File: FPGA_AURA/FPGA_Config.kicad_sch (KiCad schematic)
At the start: 31 parts, among them U1 XC7A35T-2FTG256C, U2 W25Q256JVEIQ, U3 FT2232HQ, U5 USBLC6-2SC6, U6 93LC56BT-I_SN, Y1 12MHz

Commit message: Moved to KiCAD V10 for delay.
The FPGA PCB has now been moved to KiCAD V10 to make use of the new delay features and design rules are being setup.

PCB stack-up has now been decided.
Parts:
- U2: DESCRIPTION 256M-bit Serial Flash Memory with uniform 4KB sectors and D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 -> (none)

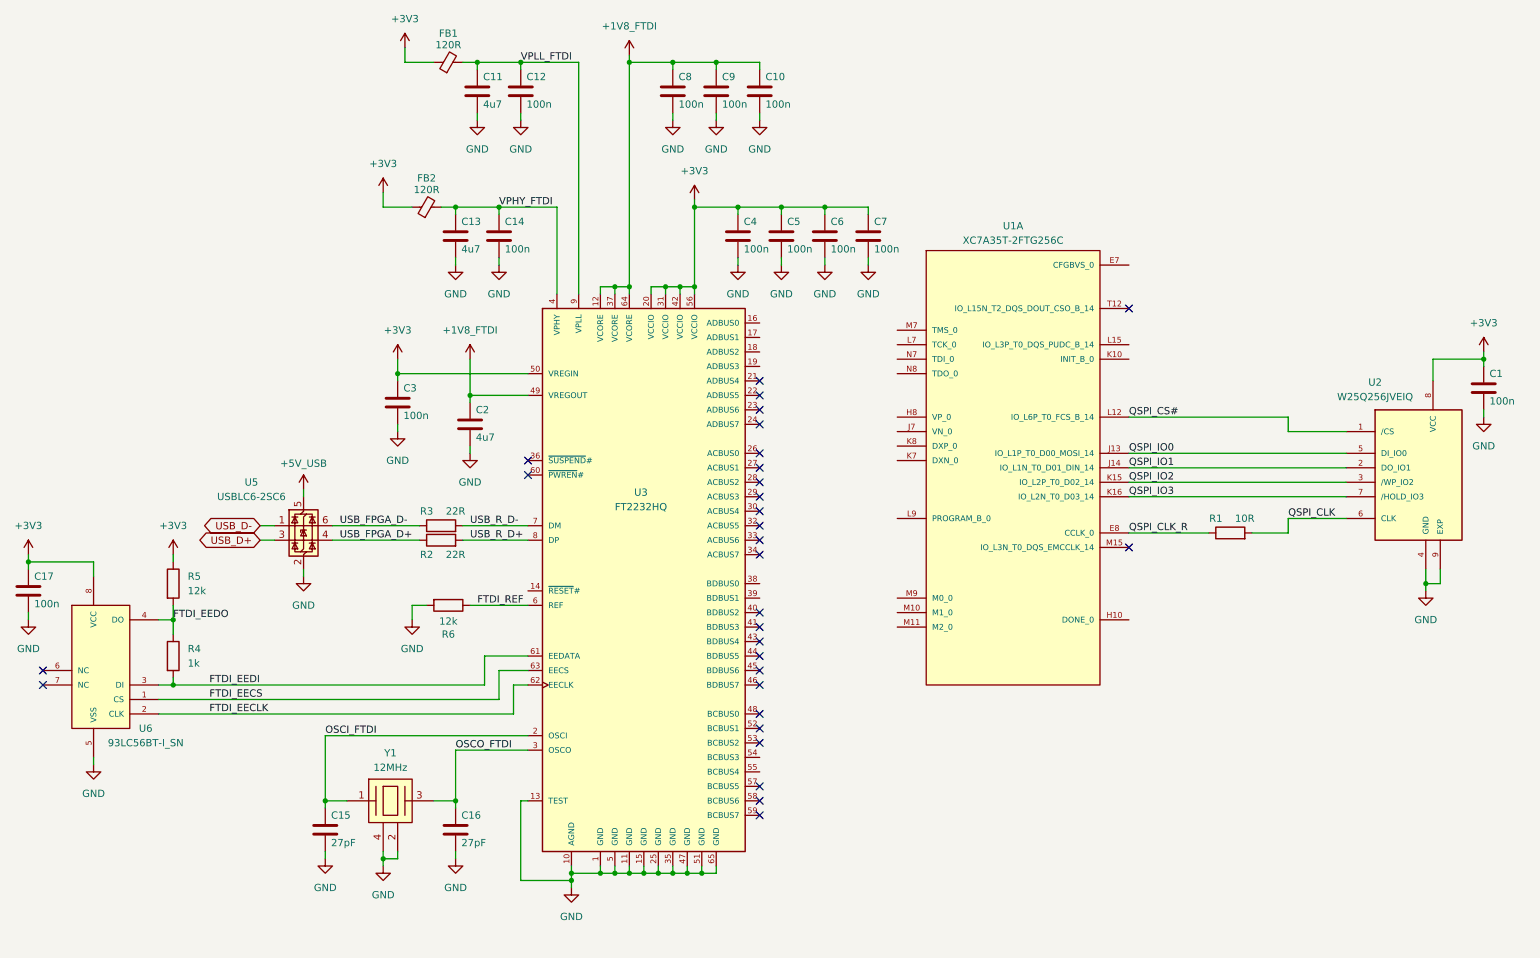
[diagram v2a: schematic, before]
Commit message: Changing stackup to 10 layers and connectors change
Development has been slow due to SI concerns with 8 layers so changing the layer count to 10 will simplify design. The picoblade/SD connector(s) are large and not high speed, so a high speed mezzanine will be used to go to a daughter board with the picoblade connectors and SD card, or other devices/protocols e.g. ADCs, COAX, IMUs, etc.
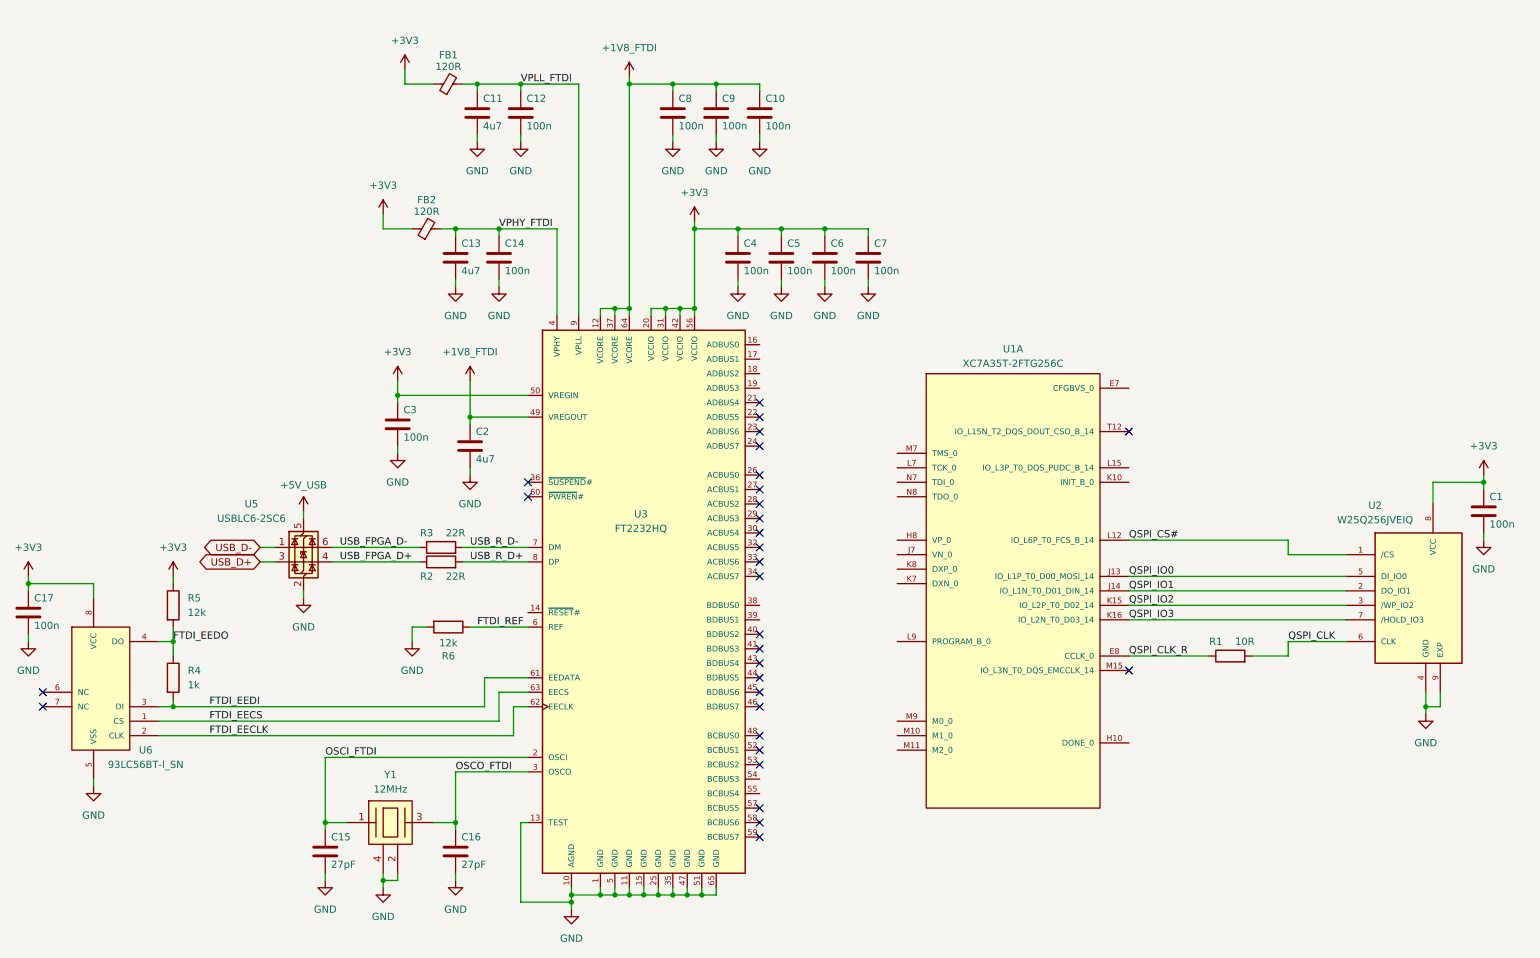
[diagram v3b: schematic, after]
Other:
- moved on the sheet: C1, C10, C11, C12, C13, C14, C15, C16, C17, C2, C3, C4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

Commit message: Continuing the FTDI
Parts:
- added D107: LED, LED_SMD:LED_0603_1608Metric, symbol Device:LED
- added R110: 200R, Resistor_SMD:R_0402_1005Metric, symbol Device:R
- added R111: 100R, Resistor_SMD:R_0402_1005Metric, symbol Device:R
- added R7: 12k, Resistor_SMD:R_0402_1005Metric, symbol Device:R
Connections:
- net +3V3: now also U1.E7 (CFGBVS_0), U1.M9 (M0_0), R110.2, R7.1
- net GND: now also U1.H8 (VP_0), U1.J7 (VN_0), U1.K7 (DXN_0), U1.K8 (DXP_0), U1.L15 (IO_L3P_T0_DQS_PUDC_B_14), U1.M10 (M1_0), U1.M11 (M2_0), D107.1 (K)
- net at U3.16 (ADBUS0): now also U1.L7 (TCK_0)
- net at U3.17 (ADBUS1): now also U1.N7 (TDI_0)
- net at U3.18 (ADBUS2): now also U1.N8 (TDO_0)
- net at U3.19 (ADBUS3): now also U1.M7 (TMS_0)
- net FTDI_TXD: now reaches U3.38 (BDBUS0)
- net FTDI_RXD: now reaches U3.39 (BDBUS1)
- net DONE_0: now reaches U1.H10 (DONE_0)
- net DONE_0: now also R110.1, R111.2
- net INIT_B_0: now reaches U1.K10 (INIT_B_0)
- net INIT_B_0: now also R7.2
- new net DONE_LED: D107.2 (A), R111.1
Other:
- moved on the sheet: C1, R1, U1A, U2
